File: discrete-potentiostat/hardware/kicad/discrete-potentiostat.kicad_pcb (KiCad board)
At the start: 4 copper layers, 24 x 22 mm, 70 parts, among them J1 ELECTRODES, J2 SWD, U1 BQ51013BRHLR, U2 MIC5205-3.3YM5, U3 nRF52832-QFAA, U4 OPA2391DGKR, U5 REF35102QDBVR, U6 MCP73832T-2ACI/OT, Y1 32MHz 8pF 10ppm

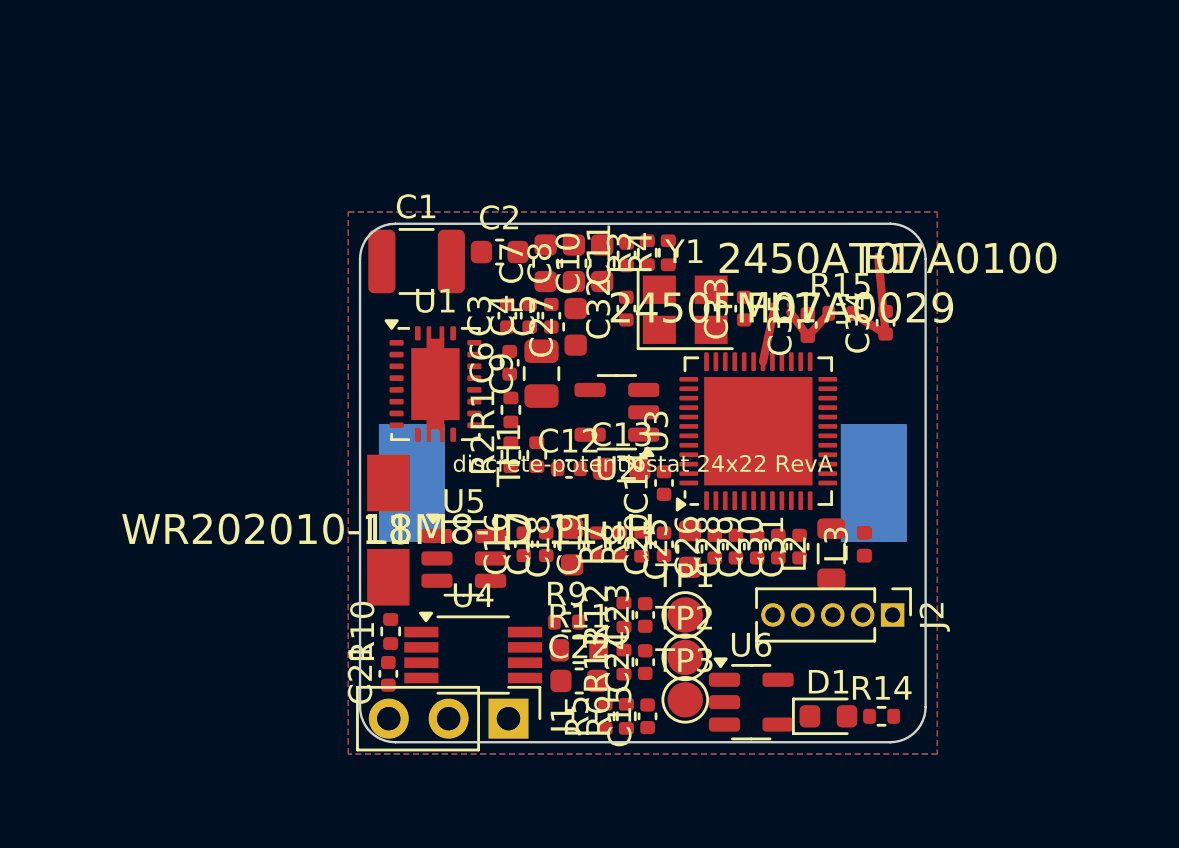
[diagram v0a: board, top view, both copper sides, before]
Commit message: Auto-route PCB: GND planes stitched, ~90% of signals routed, rules set
Custom A* grid router (generator/route_pcb.py) over F.Cu/B.Cu with via
moves, rip-up-and-reroute, long-net bottom-layer bias, and a RESUME mode
that preserves existing copper and routes only unconnected endpoints.
GND handled by 4-layer pours + shared stitching vias; RF feed untouched.

Board design rules aligned to the routed geometry (0.09 min track/clear,
0.4/0.2 via -> within JLC 4-layer capability), which reduces real DRC
electrical findings to: 39 unconnected pads (~20 links, clustered at the
charger cap bank and the nRF south-west flank), 12 clearance, 3 hole.
Full report in hardware/kicad/drc-report.txt; interactive finish guide
added to the README. Renders refreshed.

Co-Authored-By: Claude Fable 5 <noreply@anthropic.com>
Claude-Session: https://claude.ai/code/session_01GUNJUwfGKqvkZFmTaLQRu3
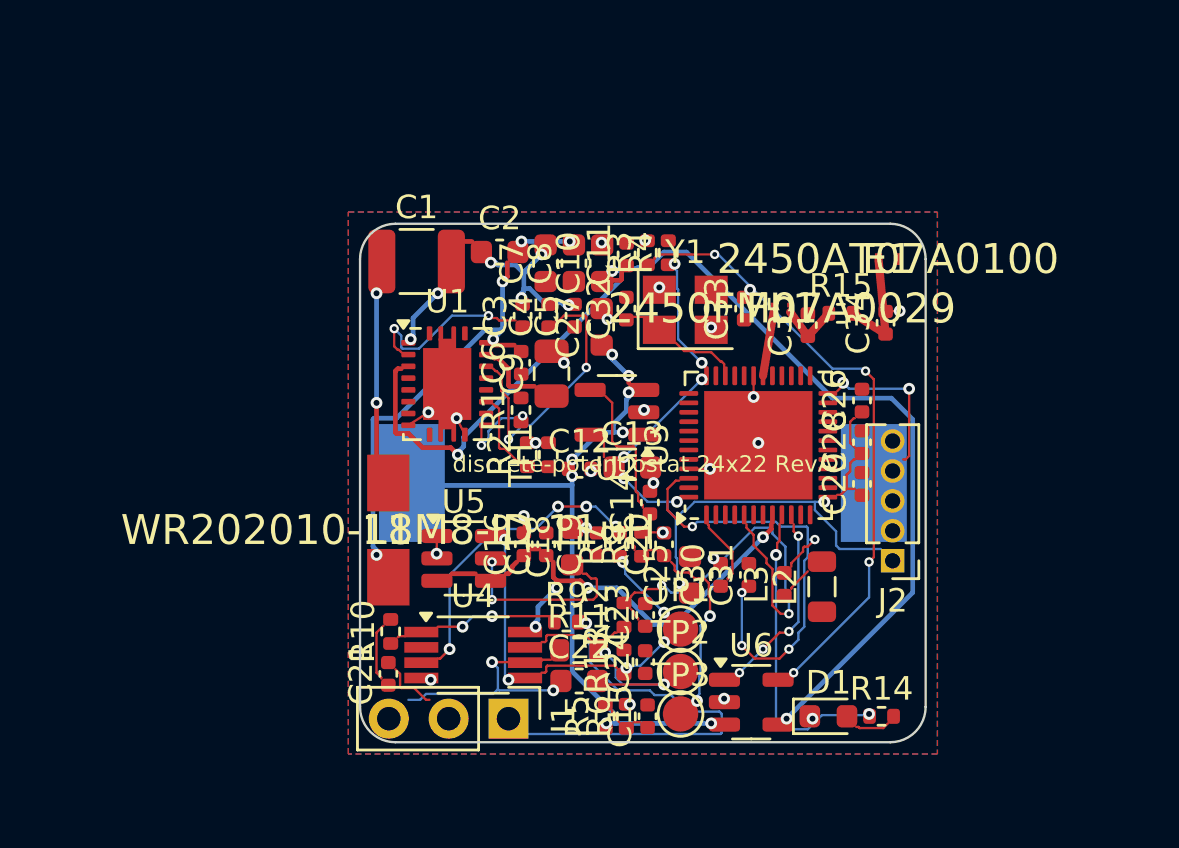
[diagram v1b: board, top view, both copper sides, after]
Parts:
- moved C26 8.80 mm to (121.3, 107.5)
- moved C28 6.95 mm to (121.3, 109.3)
- moved C29 5.18 mm to (121.3, 111.0)
- moved L3 3.80 mm to (118.0, 115.3)
- moved C30 2.73 mm to (115.3, 114.9)
- moved C31 2.46 mm to (116.5, 114.9)
- moved J2 2.30 mm to (122.6, 114.3), turned to 180 degrees
- moved L2 1.46 mm to (119.6, 115.4)
- moved C25 1.10 mm to (114.0, 114.9)
- moved C27 1.10 mm to (110.2, 104.4)
- moved C14 1.02 mm to (112.3, 111.8)
- moved C5 0.98 mm to (109.1, 103.9)
- moved C4 0.80 mm to (108.0, 103.9)
- moved R2 0.70 mm to (107.1, 109.8)
- moved C3 0.65 mm to (106.9, 103.9)
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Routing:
- net V5OUT: track 0.00 -> 48.4 mm, vias 0 -> 3
- net +3V3: track 0.00 -> 31.3 mm, vias 0 -> 8
- net +BATT: track 0.00 -> 27.6 mm, vias 0 -> 8
- net PROG: track 0.00 -> 25.5 mm, vias 0 -> 4
- net VBIAS: track 0.00 -> 20.8 mm, vias 0 -> 6
- net DEC4: track 0.00 -> 20.0 mm, vias 0 -> 5
- net AC2: track 0.00 -> 19.4 mm, vias 0 -> 5
- net CE: track 0.00 -> 17.3 mm, vias 0 -> 1
- net AFE_PWR: track 0.00 -> 17.0 mm, vias 0 -> 4
- net ADC_P: track 0.00 -> 16.7 mm, vias 0 -> 2
- net VREF: track 0.00 -> 14.8 mm, vias 0 -> 6
- net LED_R: track 0.00 -> 13.0 mm, vias 0 -> 2
- net GND: track 0.00 -> 11.6 mm, vias 0 -> 27
- net BOOT2: track 0.00 -> 11.5 mm, vias 0 -> 2
- net WE: track 0.00 -> 10.2 mm, vias 0 -> 2
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
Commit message: 6-layer PCB + solder-pad connectors: auto-routing reaches ~92%
Per user decisions: (1) J1/J2 pin headers replaced with 1.0mm round
solder pads (1.8mm pitch) for direct wire soldering - also removes THT
barrels from inner layers; (2) board upgraded 4 -> 6 layers
(L1 sig/RF, L2 GND, L3/L4 routing, L5 GND, L6 sig+battery pads).

Router upgraded to 4 routing layers with through-vias, DRC-driven todo
override for RESUME runs, self-rip protection for large nets, and design
rules baked into generation (0.09/0.09, via 0.4/0.2). Result: unrouted
links 20 (4-layer) -> 8 (6-layer); 7 clearance items; finish guide in the
README (KiCad push-and-shove, ~30min). DRC report refreshed.

Co-Authored-By: Claude Fable 5 <noreply@anthropic.com>
Claude-Session: https://claude.ai/code/session_01GUNJUwfGKqvkZFmTaLQRu3
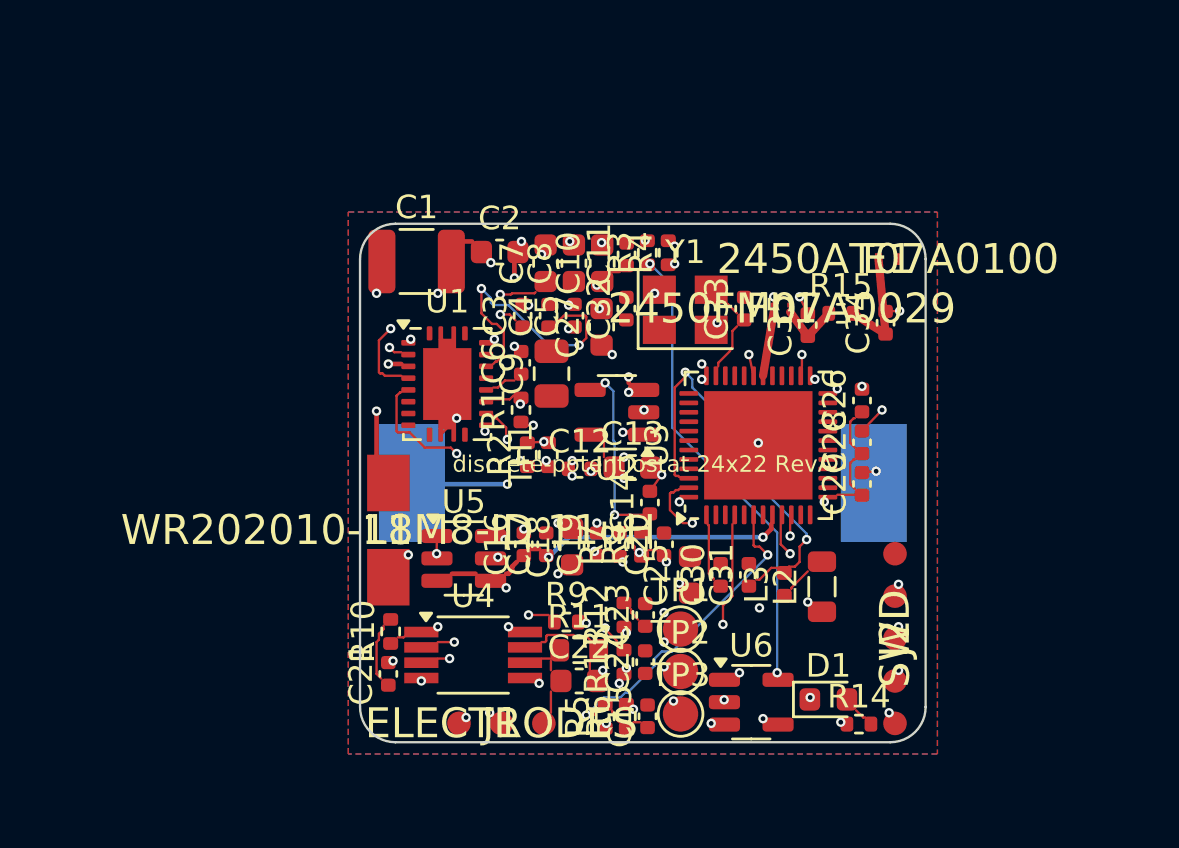
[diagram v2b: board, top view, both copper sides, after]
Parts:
- J1: footprint PinHeader_1x03_P2.54mm_Vertical -> pstat:SolderPads_1x03_D1.0mm
- J2: footprint PinHeader_1x05_P1.27mm_Vertical -> pstat:SolderPads_1x05_D1.0mm
- moved J2 3.30 mm to (122.7, 117.6), turned to 90 degrees
- moved R14 1.02 mm to (121.2, 121.2)
- moved D1 0.72 mm to (119.9, 120.2)
- moved J1 0.36 mm to (106.0, 121.2), turned to 0 degrees
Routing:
- net V5OUT: track 48.4 -> 31.8 mm
- net ADC_P: track 16.7 -> 0.57 mm, vias 2 -> 0
- net SWDIO: track 0.00 -> 15.6 mm, vias 0 -> 2
- net CHG_N: track 7.62 -> 22.1 mm
- net VBAT_DIV: track 0.92 -> 13.9 mm, vias 0 -> 2
- net SWDCLK: track 0.00 -> 12.1 mm, vias 0 -> 2
- net COMM1: track 0.00 -> 12.0 mm, vias 0 -> 2
- net CE: track 17.3 -> 6.86 mm, vias 1 -> 2
- net ADC_N: track 0.00 -> 10.4 mm, vias 0 -> 2
- net CLAMP1: track 0.00 -> 9.86 mm, vias 0 -> 2
- net DCC: track 0.00 -> 8.65 mm, vias 0 -> 2
- net WE: track 10.2 -> 1.70 mm, vias 2 -> 0
- net PROG: track 25.5 -> 19.6 mm, vias 4 -> 2
- net +3V3: track 31.3 -> 37.0 mm, vias 8 -> 9
- net RE: track 2.31 -> 7.06 mm, vias 0 -> 3
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- added copper zone on In4.Cu, net GND
- removed copper zone on In2.Cu, net GND
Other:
- copper layers 4 -> 6

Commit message: Swap op amp to LPV802 (nanopower) per user request
LPV802DGKR: 320nA/ch, 0.1pA input bias, 8kHz GBW, VSSOP-8 — same package
and standard dual pinout as the OPA2391 it replaces, so the PCB keeps its
routing (value updated in place). AFE rail drops to ~2uA total.

Trade-off documented: +/-3.5mV max offset -> +/-3.5nA fixed TIA offset at
RF=1M, removed by the existing zero-calibration step; pin-compatible
LPV812 (+/-0.3mV) noted as the precision upgrade. Netlist re-verified.

Co-Authored-By: Claude Fable 5 <noreply@anthropic.com>
Claude-Session: https://claude.ai/code/session_01GUNJUwfGKqvkZFmTaLQRu3
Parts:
- U4: value OPA2391DGKR -> LPV802DGKR
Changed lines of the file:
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@@
         (effects (font (size 1 1) (thickness 0.15)))
     )
-    (fp_text value "OPA2391DGKR" (at 0.02 2.73) (layer "F.Fab")
+    (fp_text value "LPV802DGKR" (at 0.02 2.73) (layer "F.Fab")
         (effects (font (size 1 1) (thickness 0.15)))
     )

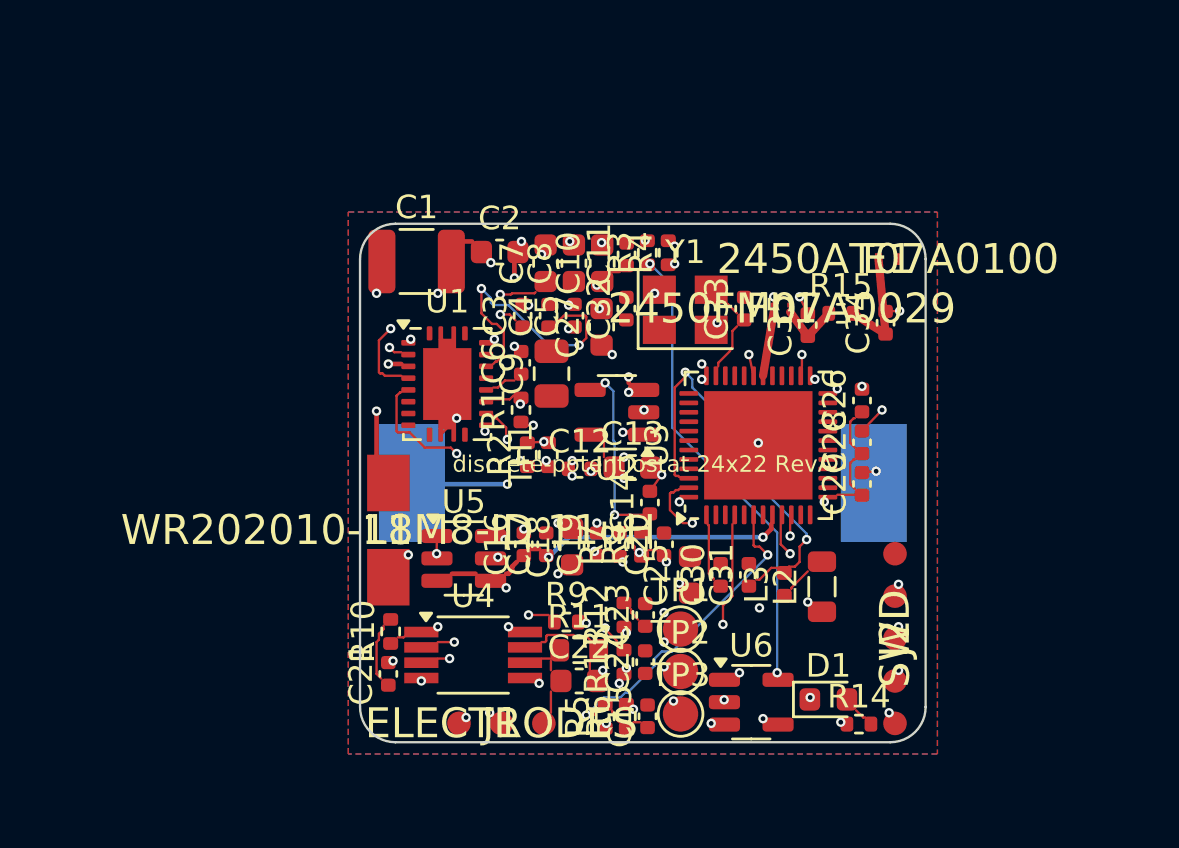
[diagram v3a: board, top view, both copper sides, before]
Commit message: Regenerate 26x24 double-sided PCB placement (routing in progress)
The previously routed board file was accidentally overwritten by a DRC
report; regenerated from gen_pcb.py (placement + zones + keepout + RF
pre-route). Full auto-route re-run follows in the next commit.

Co-Authored-By: Claude Fable 5 <noreply@anthropic.com>
Claude-Session: https://claude.ai/code/session_01GUNJUwfGKqvkZFmTaLQRu3
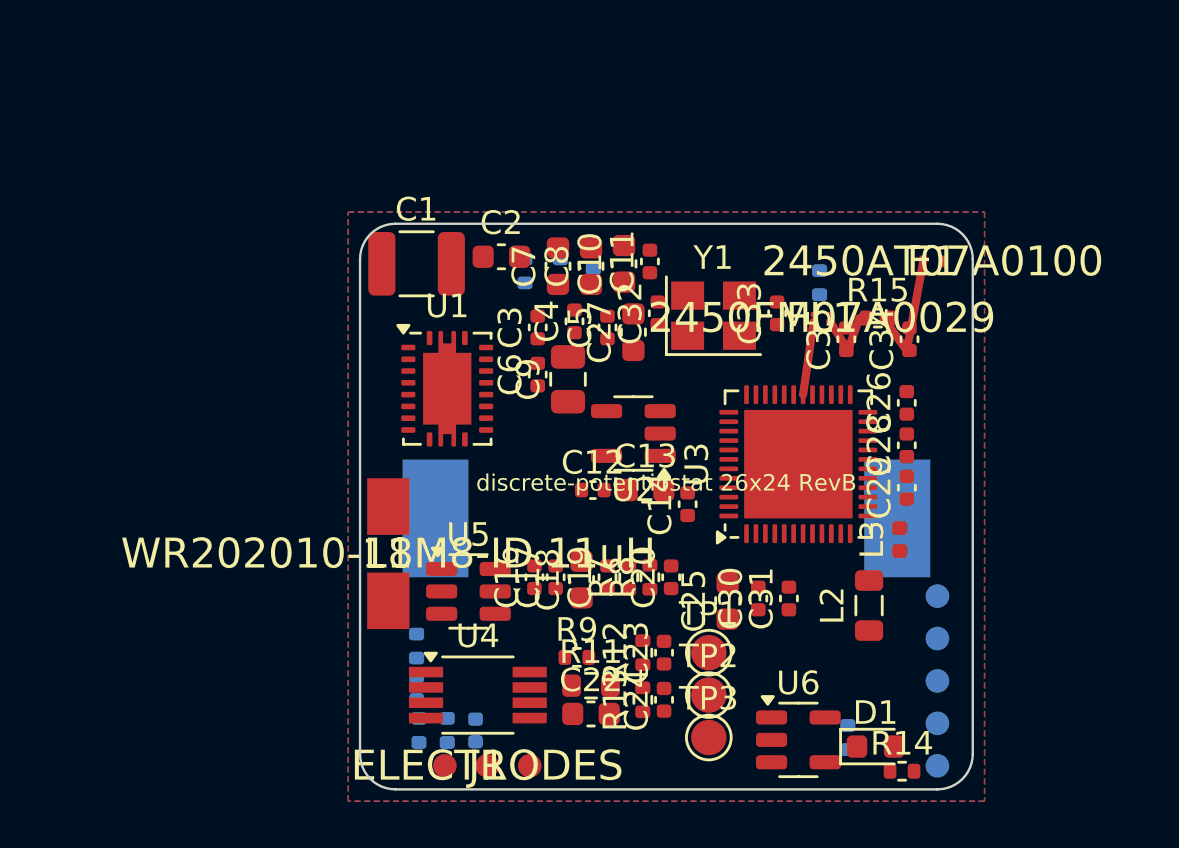
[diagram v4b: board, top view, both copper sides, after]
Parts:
- C15, C21, J2, R1, R10, R2, R3, R4, R5, R6, TH1: moved to B.Cu
- U4: value LPV802DGKR -> OPA2391DGKR
- moved R3 22.3 mm to (120.7, 121.8)
- moved TH1 8.61 mm to (109.9, 101.4)
- moved R2 7.92 mm to (108.5, 102.0)
- moved R5 7.92 mm to (102.5, 121.5)
- moved R6 7.62 mm to (103.7, 121.5)
- moved C15 7.32 mm to (104.9, 121.5)
- moved R4 6.54 mm to (119.5, 102.5)
- moved R1 5.90 mm to (107.0, 102.0)
- moved L3 5.26 mm to (122.9, 113.4)
- moved D1 2.83 mm to (121.9, 122.2)
- moved R14 2.71 mm to (123.0, 123.2)
- moved U6 2.56 mm to (118.6, 121.9)
- moved J2 2.55 mm to (124.5, 119.4)
- moved L2 2.15 mm to (121.6, 116.2)
- moved C31 1.97 mm to (118.2, 115.9)
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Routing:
- net +3V3: track 37.0 -> 0.00 mm, vias 9 -> 0
- net V5OUT: track 31.8 -> 0.00 mm, vias 3 -> 0
- net +BATT: track 27.5 -> 0.00 mm, vias 9 -> 0
- net CHG_N: track 22.1 -> 0.00 mm, vias 4 -> 0
- net PROG: track 19.6 -> 0.00 mm, vias 2 -> 0
- net VBIAS: track 17.4 -> 0.00 mm, vias 4 -> 0
- net AC2: track 17.3 -> 0.00 mm, vias 6 -> 0
- net DEC4: track 17.2 -> 0.00 mm, vias 2 -> 0
- net SWDIO: track 15.6 -> 0.00 mm, vias 2 -> 0
- net AFE_PWR: track 13.9 -> 0.00 mm, vias 4 -> 0
- net VBAT_DIV: track 13.9 -> 0.00 mm, vias 2 -> 0
- net VREF: track 12.8 -> 0.00 mm, vias 8 -> 0
- net SWDCLK: track 12.1 -> 0.00 mm, vias 2 -> 0
- net COMM1: track 12.0 -> 0.00 mm, vias 2 -> 0
- net BOOT2: track 11.9 -> 0.00 mm, vias 2 -> 0
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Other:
- board size 24 x 22 mm -> 26 x 24 mm
- board text added: "discrete-potentiostat 26x24 RevB"
- board text removed: "discrete-potentiostat 24x22 RevA"

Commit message: WIP: re-route pass for last 3 links at BQ51013B corner
Ripped RECT/V5OUT/FOD/TS corridor blockers; router re-running with
CLAMP2/BOOT2/COMM2 prioritized. Final routed board follows.

Co-Authored-By: Claude Fable 5 <noreply@anthropic.com>
Claude-Session: https://claude.ai/code/session_01GUNJUwfGKqvkZFmTaLQRu3
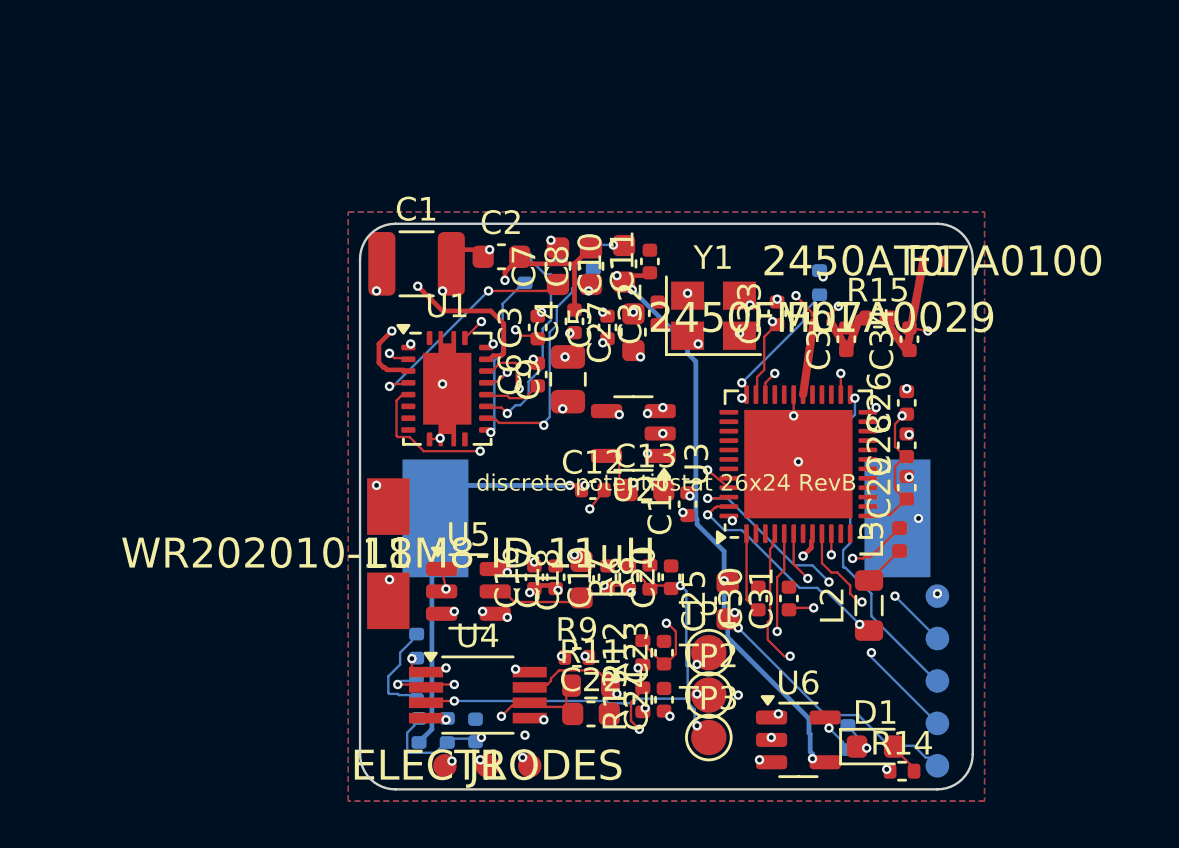
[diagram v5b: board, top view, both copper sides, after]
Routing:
- net +3V3: track 0.00 -> 44.7 mm, vias 0 -> 7
- net V5OUT: track 0.00 -> 38.2 mm, vias 0 -> 4
- net +BATT: track 0.00 -> 34.6 mm, vias 0 -> 7
- net VBAT_DIV: track 0.00 -> 23.2 mm, vias 0 -> 2
- net AC2: track 0.00 -> 22.8 mm, vias 0 -> 4
- net CHG_N: track 0.00 -> 20.9 mm, vias 0 -> 3
- net VBIAS: track 0.00 -> 18.5 mm, vias 0 -> 3
- net AFE_PWR: track 0.00 -> 17.7 mm, vias 0 -> 7
- net VREF: track 0.00 -> 17.3 mm, vias 0 -> 6
- net SWDIO: track 0.00 -> 16.6 mm, vias 0 -> 2
- net ADC_N: track 0.00 -> 15.8 mm, vias 0 -> 3
- net RECT: track 0.00 -> 15.0 mm, vias 0 -> 2
- net ADC_P: track 0.00 -> 14.7 mm, vias 0 -> 3
- net GND: track 0.00 -> 14.1 mm, vias 0 -> 30
- net SWDCLK: track 0.00 -> 13.6 mm, vias 0 -> 1
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
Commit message: PCB fully auto-routed: 0 unconnected, 0 copper DRC violations
- Re-route with net priority cracked the BQ51013B QFN corner: ripped
  RECT/V5OUT/FOD/TS corridor blockers, routed CLAMP2/BOOT2/COMM2 first,
  re-routed the ripped nets after (route_pcb.py PRIORITY env)
- GND cleanup: stitched orphan pads (U1.9/C32/R2/C23/C24) with vias,
  stitched isolated zone islands, sub-0.7mm2 slivers auto-removed
- RF feed re-routed with clearance-validated paths: ANT (U3.30->FL1)
  approaches pad from south clear of GND pads; ANT50 runs south around
  C35; ANT_FEED rounds C34 east into the chip antenna
- C1 moved +0.22/+0.46mm off the rounded board corner (was outside the
  edge-clearance arc); connectivity preserved
- Final DRC: unconnected 0, clearance 0, edge 0, isolated copper 0 -
  remaining items are silkscreen/courtyard warnings from dense placement
- Docs: kicad README final state + convergence workflow; refreshed
  drc-report.txt and top/bottom PDF renders; synced generator scripts

Co-Authored-By: Claude Fable 5 <noreply@anthropic.com>
Claude-Session: https://claude.ai/code/session_01GUNJUwfGKqvkZFmTaLQRu3
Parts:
- moved C1 0.51 mm to (102.6, 102.2)
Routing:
- net GND: track 14.1 -> 18.6 mm, vias 30 -> 45
